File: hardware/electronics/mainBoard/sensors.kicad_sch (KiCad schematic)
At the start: 3 parts, among them J16 M8S-04PFFR-SF8001, U18 LPS28DFW

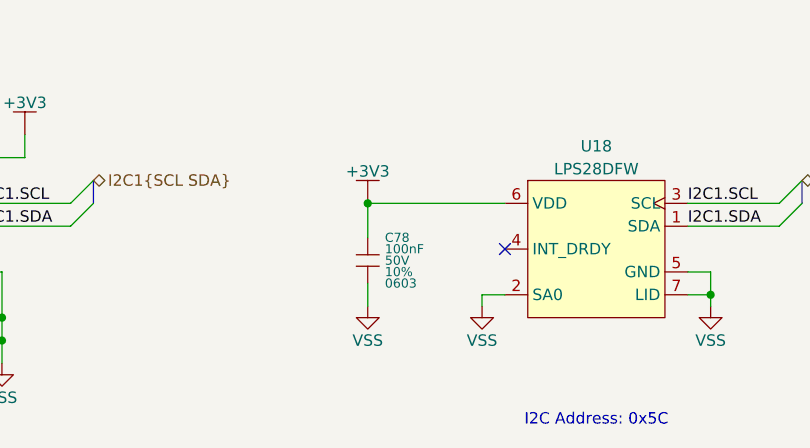
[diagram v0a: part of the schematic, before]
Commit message: updated capacitors
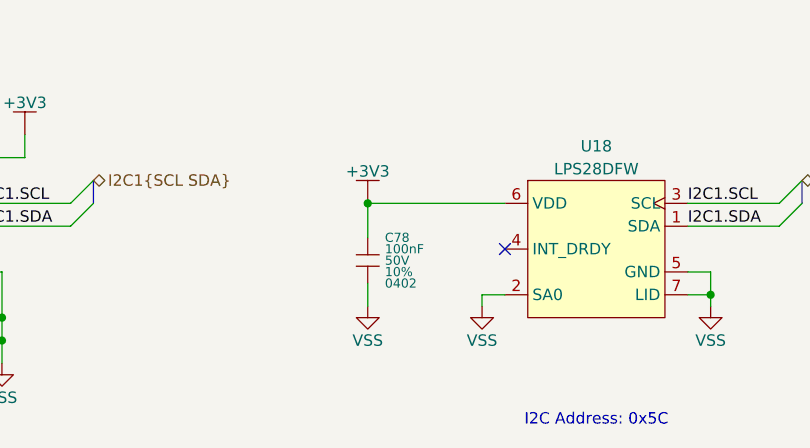
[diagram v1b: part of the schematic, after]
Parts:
- C78: DKPN 478-KAM15AR71H104KTCT-ND -> 490-GRT155R71H104KE01DCT-ND; MPN 06035C104K4T2A -> GRT155R71H104KE01D; Manufacturer KYOCERA AVX -> Murata Electronics; Package 0603 -> 0402
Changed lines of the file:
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@@
 			)
 		)
-		(property "Datasheet" "datasheets/KYOCERA-AVX-MLCCKAM.pdf"
+		(property "Datasheet" "datasheets/Murata-Electronics-GRT155R71H104KE01.pdf"
 			(at 152.4 107.315 0)
 			(effects
@@
 			)
 		)
-		(property "Description" "CAP CER 0.1UF 50V X7R 0603"
-			(at 152.4 109.22 0)
-			(effects
-				(font
-					(size 1.27 1.27)
-				)
-				(hide yes)
-			)
-		)
-		(property "Manufacturer" "KYOCERA AVX"
+		(property "Description" "CAP CER 0.1UF 50V X7R 0402"
+			(at 152.4 109.22 0)
+			(effects
+				(font
+					(size 1.27 1.27)
+				)
+				(hide yes)
+			)
+		)
+		(property "Manufacturer" "Murata Electronics"
 			(at 152.4 107.315 0)
 			(effects
@@
 			)
 		)
-		(property "MPN" "06035C104K4T2A"
+		(property "MPN" "GRT155R71H104KE01D"
 			(at 152.4 107.315 0)
 			(effects
@@
 			)
 		)
-		(property "DKPN" "478-KAM15AR71H104KTCT-ND"
+		(property "DKPN" "490-GRT155R71H104KE01DCT-ND"
 			(at 152.4 109.22 0)
 			(effects
@@
 			)
 		)
-		(property "Package" "0603"
+		(property "Package" "0402"
 			(at 154.305 111.76 0)
 			(do_not_autoplace yes)
@@
 				)
 				(justify left)
+			)
+		)
+		(property "Frequency" ""
+			(at 152.4 109.22 0)
+			(effects
+				(font
+					(size 1.27 1.27)
+				)
+			)
+		)
+		(property "Tolerace" ""
+			(at 152.4 109.22 0)
+			(effects
+				(font
+					(size 1.27 1.27)
+				)
+			)
+		)
+		(property "Trip Current" ""
+			(at 152.4 109.22 0)
+			(effects
+				(font
+					(size 1.27 1.27)
+				)
+			)
+		)
+		(property "Voltage" ""
+			(at 152.4 109.22 0)
+			(effects
+				(font
+					(size 1.27 1.27)
+				)
 			)
 		)
@@
 			)
 		)
+		(property "Frequency" ""
+			(at 101.6 107.95 0)
+			(effects
+				(font
+					(size 1.27 1.27)
+				)
+			)
+		)
+		(property "Tolerace" ""
+			(at 101.6 107.95 0)
+			(effects
+				(font
+					(size 1.27 1.27)
+				)
+			)
+		)
+		(property "Trip Current" ""
+			(at 101.6 107.95 0)
+			(effects
+				(font
+					(size 1.27 1.27)
+				)
+			)
+		)
+		(property "Voltage" ""
+			(at 101.6 107.95 0)
+			(effects
+				(font
+					(size 1.27 1.27)
+				)
+			)
+		)
 		(pin "S1"
 		)
@@
 			)
 		)
+		(property "Frequency" ""
+			(at 177.8 107.95 0)
+			(effects
+				(font
+					(size 1.27 1.27)
+				)
+			)
+		)
+		(property "Tolerace" ""
+			(at 177.8 107.95 0)
+			(effects
+				(font
+					(size 1.27 1.27)
+				)
+			)
+		)
+		(property "Trip Current" ""
+			(at 177.8 107.95 0)
+			(effects
+				(font
+					(size 1.27 1.27)
+				)
+			)
+		)
+		(property "Voltage" ""
+			(at 177.8 107.95 0)
+			(effects
+				(font
+					(size 1.27 1.27)
+				)
+			)
+		)

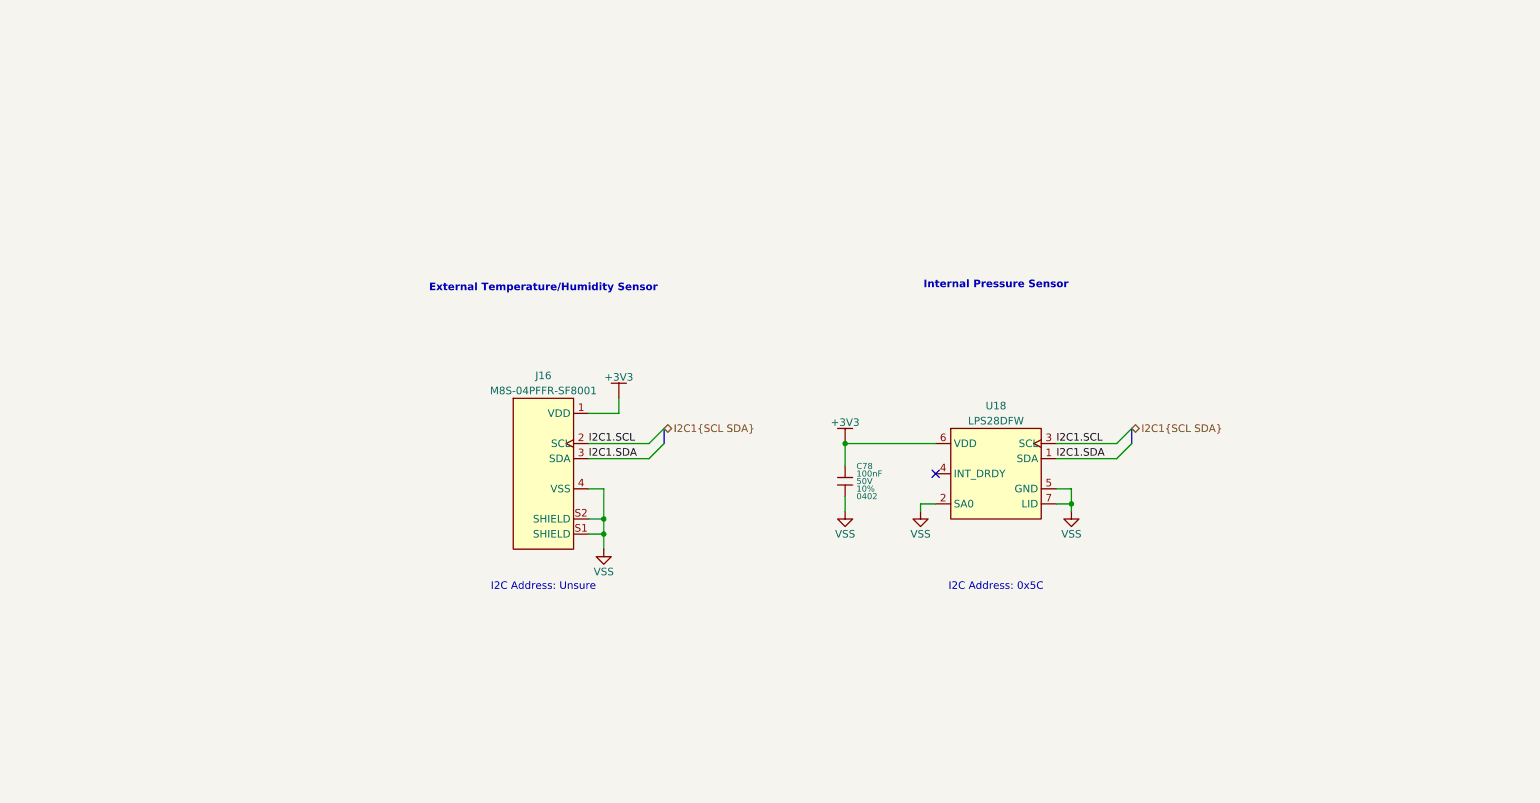
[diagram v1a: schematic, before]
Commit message: added testpoints
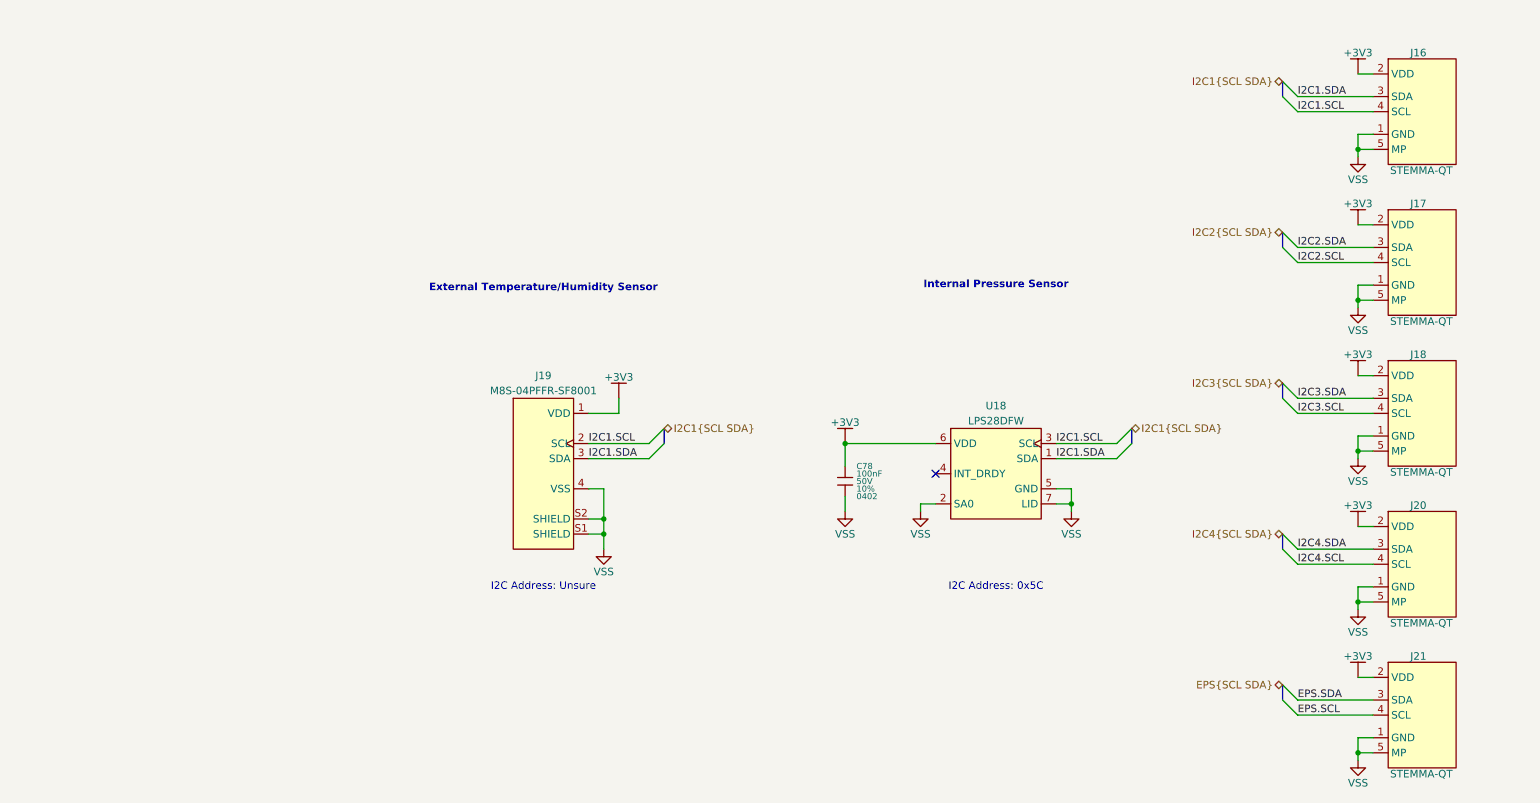
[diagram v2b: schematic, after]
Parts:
- added J16, J17, J18, J20, J21: STEMMA-QT, symbol lib_sch:STEMMA-QT_1
- U18: symbol .DS-Sensors:LPS28DFW -> lib_sch:LPS28DFW
- renumbered J16 to J19
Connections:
- net +3V3: now also J16.2 (VDD), J17.2 (VDD), J18.2 (VDD), J20.2 (VDD), J21.2 (VDD)
- net I2C1.SCL: now also J16.4 (SCL)
- net I2C1.SDA: now also J16.3 (SDA)
- net VSS: now also J16.1 (GND), J16.5 (MP), J16.6 (MP), J17.1 (GND), J17.5 (MP), J17.6 (MP), J18.1 (GND), J18.5 (MP), J18.6 (MP), J20.1 (GND), J20.5 (MP), J20.6 (MP), J21.1 (GND), J21.5 (MP), J21.6 (MP)
- new net EPS.SCL: J21.4 (SCL)
- new net EPS.SDA: J21.3 (SDA)
- new net I2C2.SCL: J17.4 (SCL)
- new net I2C2.SDA: J17.3 (SDA)
- new net I2C3.SCL: J18.4 (SCL)
- new net I2C3.SDA: J18.3 (SDA)
- new net I2C4.SCL: J20.4 (SCL)
- new net I2C4.SDA: J20.3 (SDA)

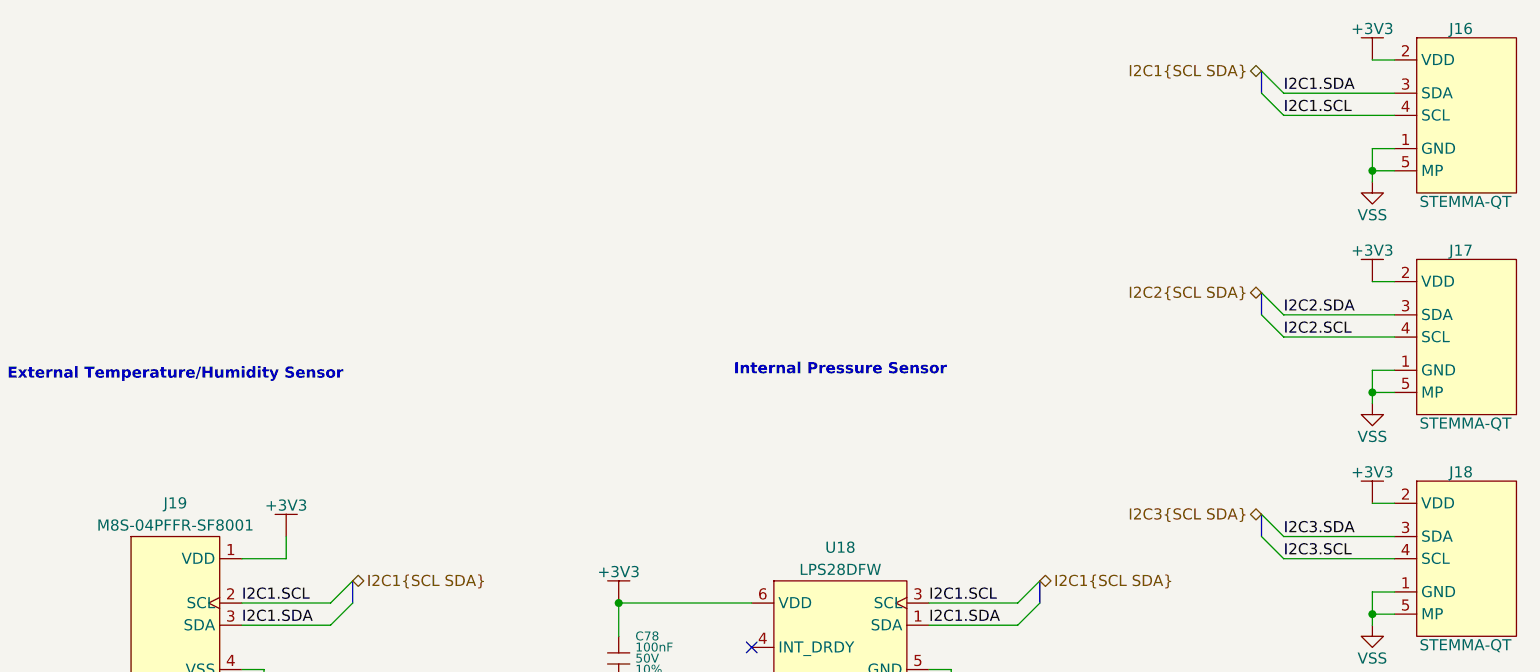
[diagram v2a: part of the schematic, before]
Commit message: updated symbol refs
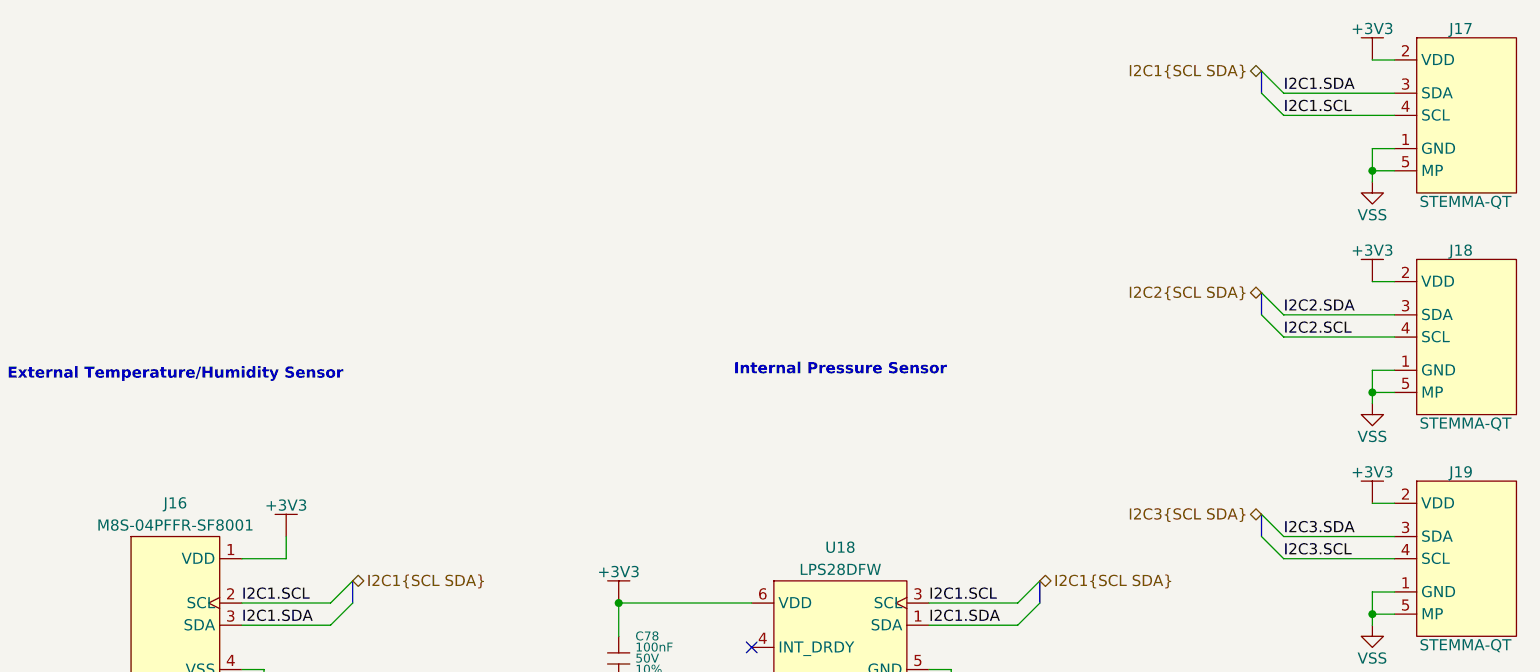
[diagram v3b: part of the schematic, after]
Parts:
- renumbered J19 to J16, J16 to J17, J17 to J18, J18 to J19
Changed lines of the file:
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@@
 		(dnp no)
 		(fields_autoplaced yes)
-		(property "Reference" "#PWR0180"
+		(property "Reference" "#PWR0187"
 			(at 238.76 54.61 0)
 			(effects
@@
 			(project "mainBoard"
 				(path "/be16e32f-2ccf-4272-9ec7-94d5fe7a55e0/4fa91b0b-0224-4171-b5d2-5ca4be681229"
-					(reference "#PWR0180")
+					(reference "#PWR0187")
 					(unit 1)
 				)
@@
 		(dnp no)
 		(fields_autoplaced yes)
-		(property "Reference" "#PWR0191"
+		(property "Reference" "#PWR0180"
 			(at 111.76 120.65 0)
 			(effects
@@
 			(project "mainBoard"
 				(path "/be16e32f-2ccf-4272-9ec7-94d5fe7a55e0/4fa91b0b-0224-4171-b5d2-5ca4be681229"
-					(reference "#PWR0191")
+					(reference "#PWR0180")
 					(unit 1)
 				)
@@
 		(dnp no)
 		(fields_autoplaced yes)
-		(property "Reference" "J17"
+		(property "Reference" "J18"
 			(at 248.92 62.484 0)
 			(do_not_autoplace yes)
@@
 			(project "mainBoard"
 				(path "/be16e32f-2ccf-4272-9ec7-94d5fe7a55e0/4fa91b0b-0224-4171-b5d2-5ca4be681229"
-					(reference "J17")
+					(reference "J18")
 					(unit 1)
 				)
@@
 		(dnp no)
 		(fields_autoplaced yes)
-		(property "Reference" "J16"
+		(property "Reference" "J17"
 			(at 248.92 37.084 0)
 			(do_not_autoplace yes)
@@
 			(project "mainBoard"
 				(path "/be16e32f-2ccf-4272-9ec7-94d5fe7a55e0/4fa91b0b-0224-4171-b5d2-5ca4be681229"
-					(reference "J16")
+					(reference "J17")
 					(unit 1)
 				)
@@
 		(dnp no)
 		(fields_autoplaced yes)
-		(property "Reference" "J18"
+		(property "Reference" "J19"
 			(at 248.92 87.884 0)
 			(do_not_autoplace yes)
@@
 			(project "mainBoard"
 				(path "/be16e32f-2ccf-4272-9ec7-94d5fe7a55e0/4fa91b0b-0224-4171-b5d2-5ca4be681229"
-					(reference "J18")
+					(reference "J19")
 					(unit 1)
 				)
@@
 		(dnp no)
 		(fields_autoplaced yes)
-		(property "Reference" "#PWR0192"
+		(property "Reference" "#PWR0193"
 			(at 238.76 130.81 0)
 			(effects
@@
 			(project "mainBoard"
 				(path "/be16e32f-2ccf-4272-9ec7-94d5fe7a55e0/4fa91b0b-0224-4171-b5d2-5ca4be681229"
-					(reference "#PWR0192")
+					(reference "#PWR0193")
 					(unit 1)
 				)
@@
 		(dnp no)
 		(fields_autoplaced yes)
-		(property "Reference" "#PWR0183"
+		(property "Reference" "#PWR0190"
 			(at 238.76 91.44 0)
 			(effects
@@
 			(project "mainBoard"
 				(path "/be16e32f-2ccf-4272-9ec7-94d5fe7a55e0/4fa91b0b-0224-4171-b5d2-5ca4be681229"
-					(reference "#PWR0183")
+					(reference "#PWR0190")
 					(unit 1)
 				)
@@
 		(dnp no)
 		(fields_autoplaced yes)
-		(property "Reference" "#PWR0194"
+		(property "Reference" "#PWR0195"
 			(at 238.76 156.21 0)
 			(effects
@@
 			(project "mainBoard"
 				(path "/be16e32f-2ccf-4272-9ec7-94d5fe7a55e0/4fa91b0b-0224-4171-b5d2-5ca4be681229"
-					(reference "#PWR0194")
+					(reference "#PWR0195")
 					(unit 1)
 				)
@@
 		(dnp no)
 		(fields_autoplaced yes)
-		(property "Reference" "#PWR0193"
+		(property "Reference" "#PWR0194"
 			(at 238.76 142.24 0)
 			(effects
@@
 			(project "mainBoard"
 				(path "/be16e32f-2ccf-4272-9ec7-94d5fe7a55e0/4fa91b0b-0224-4171-b5d2-5ca4be681229"
-					(reference "#PWR0193")
+					(reference "#PWR0194")
 					(unit 1)
 				)
@@
 		(dnp no)
 		(fields_autoplaced yes)
-		(property "Reference" "#PWR0182"
+		(property "Reference" "#PWR0189"
 			(at 238.76 80.01 0)
 			(effects
@@
 			(project "mainBoard"
 				(path "/be16e32f-2ccf-4272-9ec7-94d5fe7a55e0/4fa91b0b-0224-4171-b5d2-5ca4be681229"
-					(reference "#PWR0182")
+					(reference "#PWR0189")
 					(unit 1)
 				)
@@
 		(dnp no)
 		(fields_autoplaced yes)
-		(property "Reference" "#PWR0181"
+		(property "Reference" "#PWR0188"
 			(at 238.76 66.04 0)
 			(effects
@@
 			(project "mainBoard"
 				(path "/be16e32f-2ccf-4272-9ec7-94d5fe7a55e0/4fa91b0b-0224-4171-b5d2-5ca4be681229"
-					(reference "#PWR0181")
+					(reference "#PWR0188")
 					(unit 1)
 				)
@@
 		(dnp no)
 		(fields_autoplaced yes)
-		(property "Reference" "#PWR0187"
+		(property "Reference" "#PWR0183"
 			(at 152.4 114.3 0)
 			(effects
@@
 			(project "mainBoard"
 				(path "/be16e32f-2ccf-4272-9ec7-94d5fe7a55e0/4fa91b0b-0224-4171-b5d2-5ca4be681229"
-					(reference "#PWR0187")
+					(reference "#PWR0183")
 					(unit 1)
 				)
@@
 		(dnp no)
 		(fields_autoplaced yes)
-		(property "Reference" "#PWR0186"
+		(property "Reference" "#PWR0191"
 			(at 238.76 105.41 0)
 			(effects
@@
 			(project "mainBoard"
 				(path "/be16e32f-2ccf-4272-9ec7-94d5fe7a55e0/4fa91b0b-0224-4171-b5d2-5ca4be681229"
-					(reference "#PWR0186")
+					(reference "#PWR0191")
 					(unit 1)
 				)
@@
 		(dnp no)
 		(fields_autoplaced yes)
-		(property "Reference" "#PWR0184"
+		(property "Reference" "#PWR0181"
 			(at 114.3 95.25 0)
 			(effects
@@
 			(project "mainBoard"
 				(path "/be16e32f-2ccf-4272-9ec7-94d5fe7a55e0/4fa91b0b-0224-4171-b5d2-5ca4be681229"
-					(reference "#PWR0184")
+					(reference "#PWR0181")
 					(unit 1)
 				)
@@
 		(dnp no)
 		(fields_autoplaced yes)
-		(property "Reference" "J19"
+		(property "Reference" "J16"
 			(at 101.6 91.44 0)
 			(do_not_autoplace yes)
@@
 			(project "mainBoard"
 				(path "/be16e32f-2ccf-4272-9ec7-94d5fe7a55e0/4fa91b0b-0224-4171-b5d2-5ca4be681229"
-					(reference "J19")
+					(reference "J16")
 					(unit 1)
 				)
@@
 		(dnp no)
 		(fields_autoplaced yes)
-		(property "Reference" "#PWR0190"
+		(property "Reference" "#PWR0192"
 			(at 238.76 116.84 0)
 			(effects
@@
 			(project "mainBoard"
 				(path "/be16e32f-2ccf-4272-9ec7-94d5fe7a55e0/4fa91b0b-0224-4171-b5d2-5ca4be681229"
-					(reference "#PWR0190")
+					(reference "#PWR0192")
 					(unit 1)
 				)
@@
 		(dnp no)
 		(fields_autoplaced yes)
-		(property "Reference" "#PWR0189"
+		(property "Reference" "#PWR0185"
 			(at 190.5 114.3 0)
 			(effects
@@
 			(project "mainBoard"
 				(path "/be16e32f-2ccf-4272-9ec7-94d5fe7a55e0/4fa91b0b-0224-4171-b5d2-5ca4be681229"
-					(reference "#PWR0189")
+					(reference "#PWR0185")
 					(unit 1)
 				)
@@
 		(dnp no)
 		(fields_autoplaced yes)
-		(property "Reference" "#PWR0185"
+		(property "Reference" "#PWR0182"
 			(at 152.4 102.87 0)
 			(effects
@@
 			(project "mainBoard"
 				(path "/be16e32f-2ccf-4272-9ec7-94d5fe7a55e0/4fa91b0b-0224-4171-b5d2-5ca4be681229"
-					(reference "#PWR0185")
+					(reference "#PWR0182")
 					(unit 1)
 				)
@@
 		(dnp no)
 		(fields_autoplaced yes)
-		(property "Reference" "#PWR0188"
+		(property "Reference" "#PWR0184"
 			(at 165.1 114.3 0)
 			(effects
@@
 			(project "mainBoard"
 				(path "/be16e32f-2ccf-4272-9ec7-94d5fe7a55e0/4fa91b0b-0224-4171-b5d2-5ca4be681229"
-					(reference "#PWR0188")
+					(reference "#PWR0184")
 					(unit 1)
 				)
@@
 		(dnp no)
 		(fields_autoplaced yes)
-		(property "Reference" "#PWR0179"
+		(property "Reference" "#PWR0186"
 			(at 238.76 40.64 0)
 			(effects
@@
 			(project "mainBoard"
 				(path "/be16e32f-2ccf-4272-9ec7-94d5fe7a55e0/4fa91b0b-0224-4171-b5d2-5ca4be681229"
-					(reference "#PWR0179")
-					(unit 1)
-				)
+					(reference "#PWR0186")
+					(unit 1)
+				)
